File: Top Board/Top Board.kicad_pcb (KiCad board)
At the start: 2 copper layers, 88.9 x 27.9 mm, 5 parts

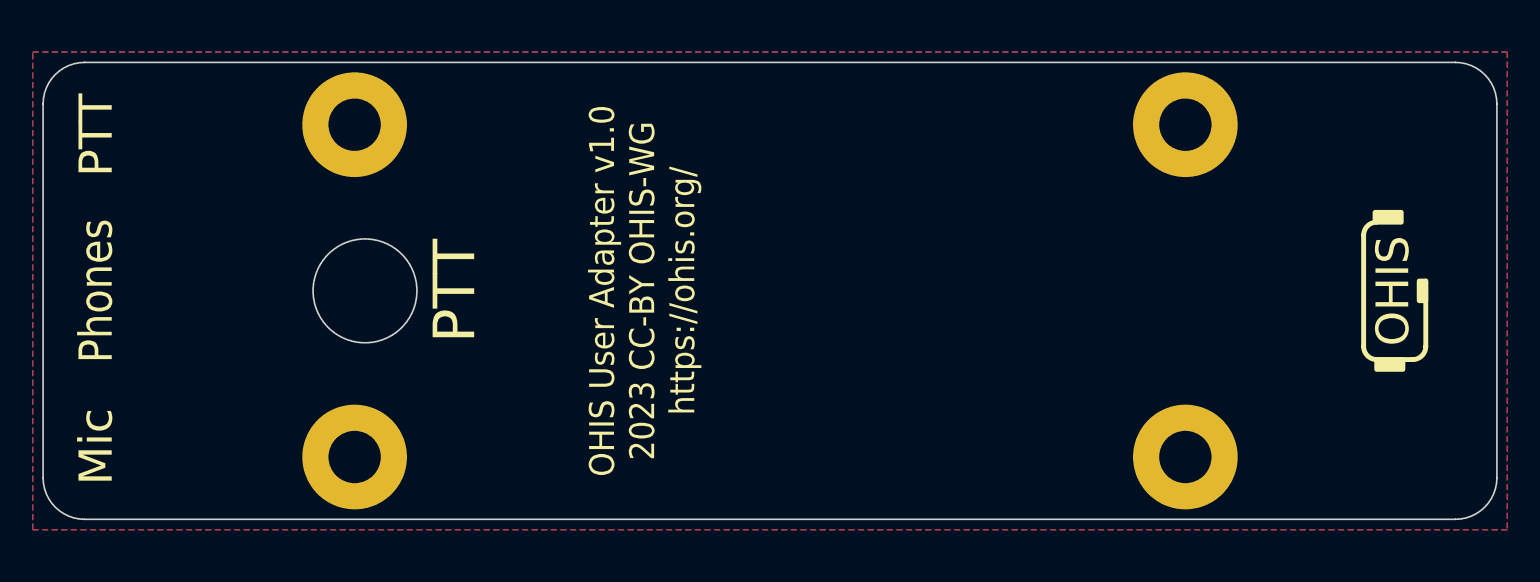
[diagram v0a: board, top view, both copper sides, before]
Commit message: Fixed silkscreen art, added trimpot. #1
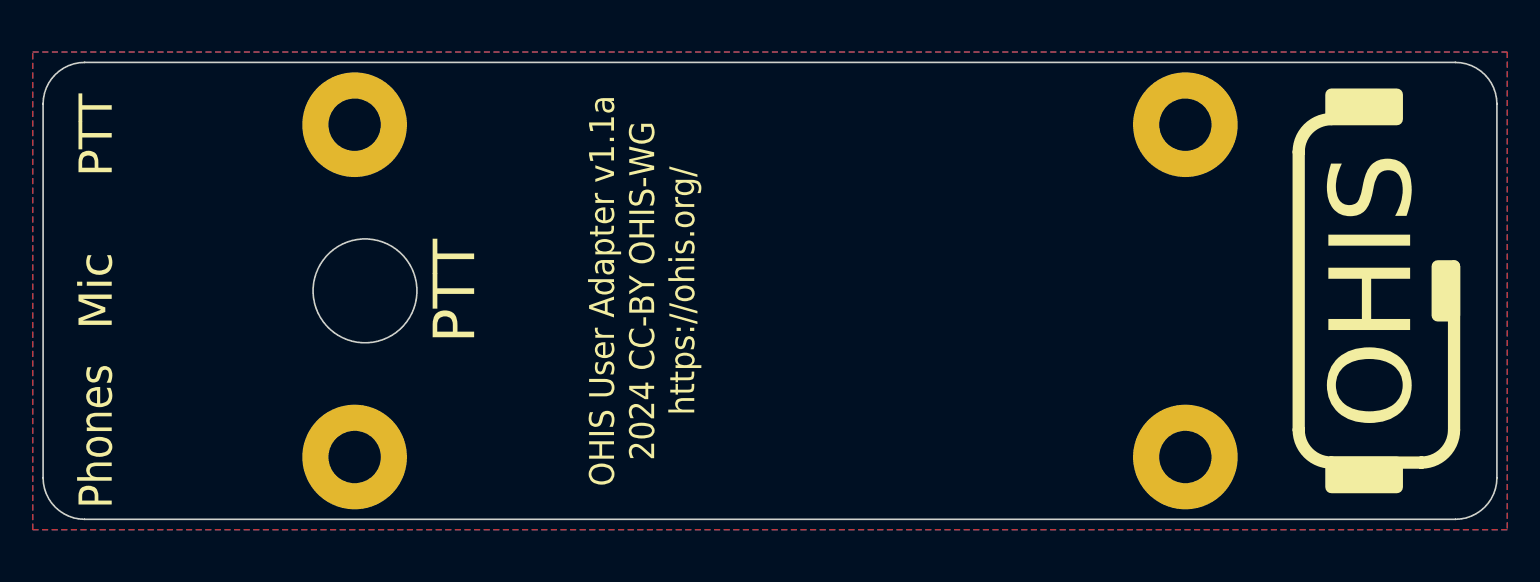
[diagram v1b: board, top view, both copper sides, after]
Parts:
- G1: footprint Libraries:Logo_OHIS_Medium -> Libraries:Logo_OHIS_Large
- moved G1 1.27 mm to (144.8, 76.2)
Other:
- board text added: "JLCJLCJLCJLC"
- board text added: "OHIS User Adapter v1.1a 2024 CC-BY OHIS-WG https://ohis.org/"
- board text removed: "OHIS User Adapter v1.0 2023 CC-BY OHIS-WG https://ohis.org/"
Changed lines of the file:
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@@
       (net 1 "GND") (pinfunction "1") (pintype "input"))
   )
-  (footprint "Libraries:Logo_OHIS_Medium" (layer "F.Cu")
-    (at 146.05 76.2 90)
+  (footprint "Libraries:Logo_OHIS_Large" (layer "F.Cu")
+    (at 144.78 76.2 90)
     (property "Sheetfile" "Top Board.kicad_sch")
     (property "Sheetname" "")
@@
     )
     (fp_text user "OHIS" (at 0 0 90 unlocked) (layer "F.SilkS")
-        (effects (font (size 2 2) (thickness 0.3)))
+        (effects (font (size 5 5) (thickness 0.75)))
     )
     (fp_text user "${REFERENCE}" (at 0 2.5 90 unlocked) (layer "F.Fab") hide
         (effects (font (size 1 1) (thickness 0.15)))
     )
-    (fp_line (start -4.200001 1.2) (end -4.2 -1)
-      (stroke (width 0.3) (type solid)) (layer "F.SilkS"))
-    (fp_line (start 0.6 2) (end -3.400001 2)
-      (stroke (width 0.3) (type solid)) (layer "F.SilkS"))
-    (fp_line (start 3.4 -1.8) (end -3.4 -1.8)
-      (stroke (width 0.3) (type solid)) (layer "F.SilkS"))
-    (fp_rect (start -4.2 0.6) (end -4.8 -1)
-      (stroke (width 0.3) (type solid)) (fill solid) (layer "F.SilkS"))
-    (fp_rect (start 0.6 2) (end -0.6 1.6)
-      (stroke (width 0.3) (type solid)) (fill solid) (layer "F.SilkS"))
-    (fp_rect (start 4.8 0.5) (end 4.2 -1.1)
-      (stroke (width 0.3) (type solid)) (fill solid) (layer "F.SilkS"))
-    (fp_arc (start -4.2 -1) (mid -3.965685 -1.565685) (end -3.4 -1.8)
-      (stroke (width 0.3) (type solid)) (layer "F.SilkS"))
-    (fp_arc (start -3.400001 2) (mid -3.965686 1.765685) (end -4.200001 1.2)
-      (stroke (width 0.3) (type solid)) (layer "F.SilkS"))
-    (fp_arc (start 3.4 -1.8) (mid 3.965685 -1.565685) (end 4.2 -1)
-      (stroke (width 0.3) (type solid)) (layer "F.SilkS"))
+    (fp_line (start -10.5 -2.5) (end -10.5 2.999999)
+      (stroke (width 0.75) (type solid)) (layer "F.SilkS"))
+    (fp_line (start 1.5 5) (end -8.499999 4.999999)
+      (stroke (width 0.75) (type solid)) (layer "F.SilkS"))
+    (fp_line (start 8.499999 -4.499999) (end -8.5 -4.5)
+      (stroke (width 0.75) (type solid)) (layer "F.SilkS"))
+    (fp_rect (start -10.5 -2.5) (end -12 1.5)
+      (stroke (width 0.75) (type solid)) (fill solid) (layer "F.SilkS"))
+    (fp_rect (start 1.5 4) (end -1.5 5)
+      (stroke (width 0.75) (type solid)) (fill solid) (layer "F.SilkS"))
+    (fp_rect (start 11.999999 -2.499999) (end 10.499999 1.500001)
+      (stroke (width 0.75) (type solid)) (fill solid) (layer "F.SilkS"))
+    (fp_arc (start -10.5 -2.5) (mid -9.914214 -3.914214) (end -8.5 -4.5)
+      (stroke (width 0.75) (type solid)) (layer "F.SilkS"))
+    (fp_arc (start -8.499999 4.999999) (mid -9.914213 4.414213) (end -10.499999 2.999999)
+      (stroke (width 0.75) (type solid)) (layer "F.SilkS"))
+    (fp_arc (start 8.499999 -4.499999) (mid 9.914213 -3.914213) (end 10.499999 -2.499999)
+      (stroke (width 0.75) (type solid)) (layer "F.SilkS"))
   )
   (footprint "MountingHole:MountingHole_3.2mm_M3_Pad" locked (layer "F.Cu")
@@
   (gr_arc locked (start 149.86 62.23) (mid 151.656051 62.973949) (end 152.4 64.77)
     (stroke (width 0.1) (type default)) (layer "Edge.Cuts"))
-  (gr_text "Mic" (at 67.945 85.725 90) (layer "F.SilkS")
+  (gr_text "JLCJLCJLCJLC" (at 107.95 76.2) (layer "B.SilkS")
+    (effects (font (size 1.524 1.397) (thickness 0.2032)) (justify mirror))
+  )
+  (gr_text "Mic" (at 67.945 76.2 90) (layer "F.SilkS")
     (effects (font (size 2.032 2.032) (thickness 0.254)) (justify bottom))
   )
-  (gr_text "OHIS User Adapter v1.0\n2023 CC-BY OHIS-WG\nhttps://ohis.org/" (at 103.505 76.2 90) (layer "F.SilkS")
+  (gr_text "OHIS User Adapter v1.1a\n2024 CC-BY OHIS-WG\nhttps://ohis.org/" (at 103.505 76.2 90) (layer "F.SilkS")
     (effects (font (size 1.524 1.397) (thickness 0.2032)) (justify bottom))
   )
-  (gr_text "Phones" (at 67.945 76.2 90) (layer "F.SilkS")
+  (gr_text "Phones" (at 67.945 85.09 90) (layer "F.SilkS")
     (effects (font (size 2.032 1.778) (thickness 0.254)) (justify bottom))
   )

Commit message: Cleaned up board, moved jumpers to right-angle at board edge.
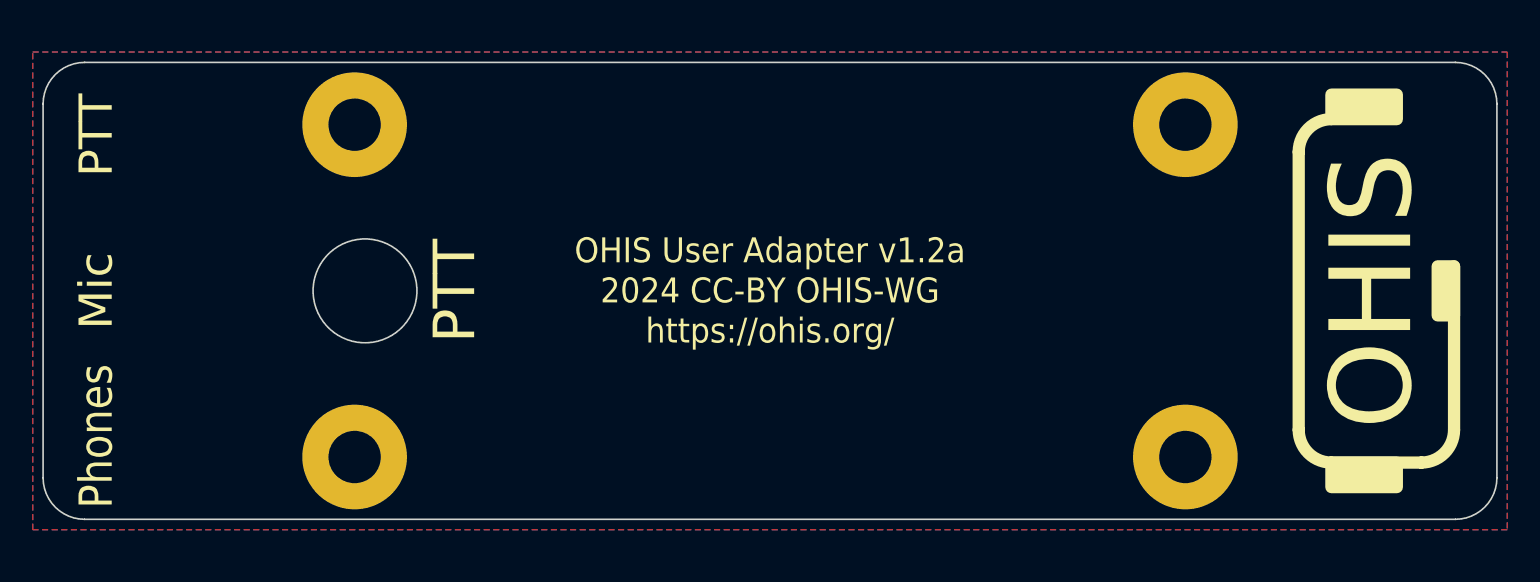
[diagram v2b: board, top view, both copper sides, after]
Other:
- board text added: "OHIS User Adapter v1.2a 2024 CC-BY OHIS-WG https://ohis.org/"
- board text removed: "OHIS User Adapter v1.1a 2024 CC-BY OHIS-WG https://ohis.org/"
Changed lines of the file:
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@@
       (net 1 "GND") (pinfunction "1") (pintype "input"))
   )
-  (gr_rect (start 140.335 67.945) (end 151.13 84.455)
+  (gr_rect (start 140.335 67.945) (end 152.4 84.455)
     (stroke (width 0.15) (type solid)) (fill solid) (layer "B.Mask"))
   (gr_line (start 158.115 76.2) (end 57.15 76.2)
@@
     (effects (font (size 2.032 2.032) (thickness 0.254)) (justify bottom))
   )
-  (gr_text "OHIS User Adapter v1.1a\n2024 CC-BY OHIS-WG\nhttps://ohis.org/" (at 103.505 76.2 90) (layer "F.SilkS")
-    (effects (font (size 1.524 1.397) (thickness 0.2032)) (justify bottom))
+  (gr_text "OHIS User Adapter v1.2a\n2024 CC-BY OHIS-WG\nhttps://ohis.org/" (at 107.95 76.2) (layer "F.SilkS")
+    (effects (font (size 1.524 1.397) (thickness 0.2032)))
   )
   (gr_text "Phones" (at 67.945 85.09 90) (layer "F.SilkS")
@@
     (pts (xy 83.185 76.2) (xy 63.5 76.2))
     (height 17.78)
-    (gr_text "0.7750 in" (at 73.3425 57.27) (layer "Dwgs.User")
+    (gr_text "19.6850 mm" (at 73.3425 57.27) (layer "Dwgs.User")
       (effects (font (size 1 1) (thickness 0.15)))
     )
@@
     (pts (xy 63.5 76.2) (xy 63.5 85.725))
     (height 2.54)
-    (gr_text "0.3750 in" (at 59.81 80.9625 90) (layer "Dwgs.User")
+    (gr_text "9.5250 mm" (at 59.81 80.9625 90) (layer "Dwgs.User")
       (effects (font (size 1 1) (thickness 0.15)))
     )
@@
     (pts (xy 63.5 76.2) (xy 63.5 66.675))
     (height -2.54)
-    (gr_text "0.3750 in" (at 59.81 71.4375 90) (layer "Dwgs.User")
+    (gr_text "9.5250 mm" (at 59.81 71.4375 90) (layer "Dwgs.User")
       (effects (font (size 1 1) (thickness 0.15)))
     )

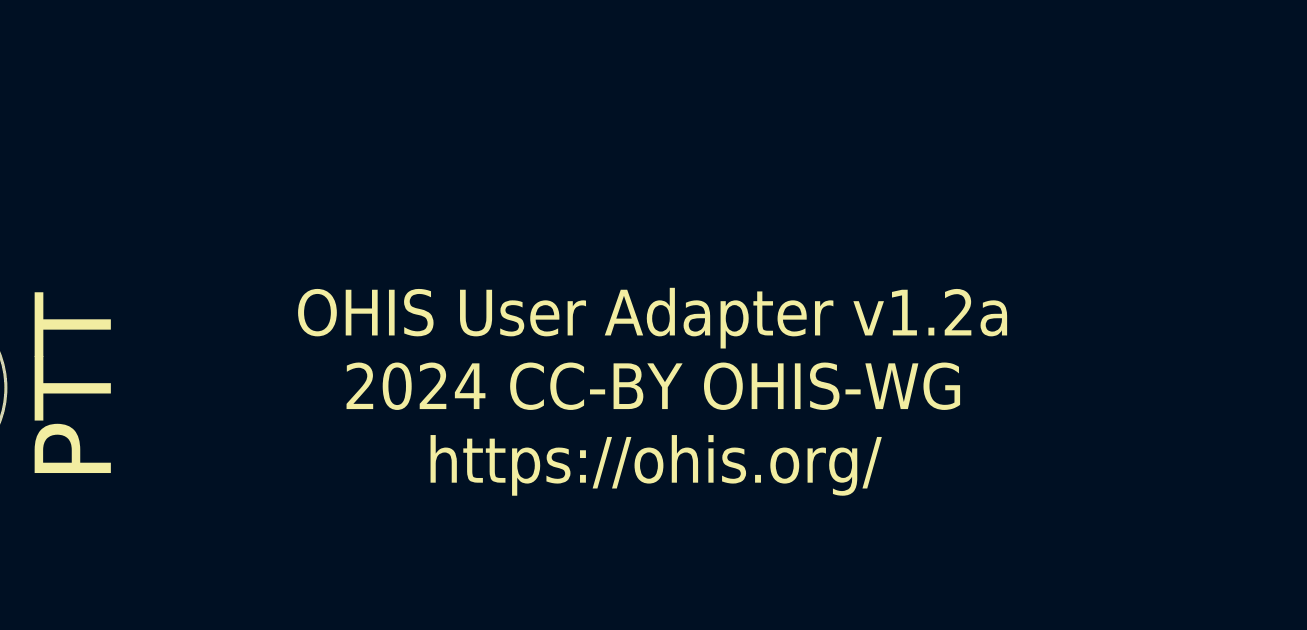
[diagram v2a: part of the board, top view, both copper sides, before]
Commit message: Halibut ordering next batch. Upping version on top/bottom to v1.3a. KiCAD 8.0
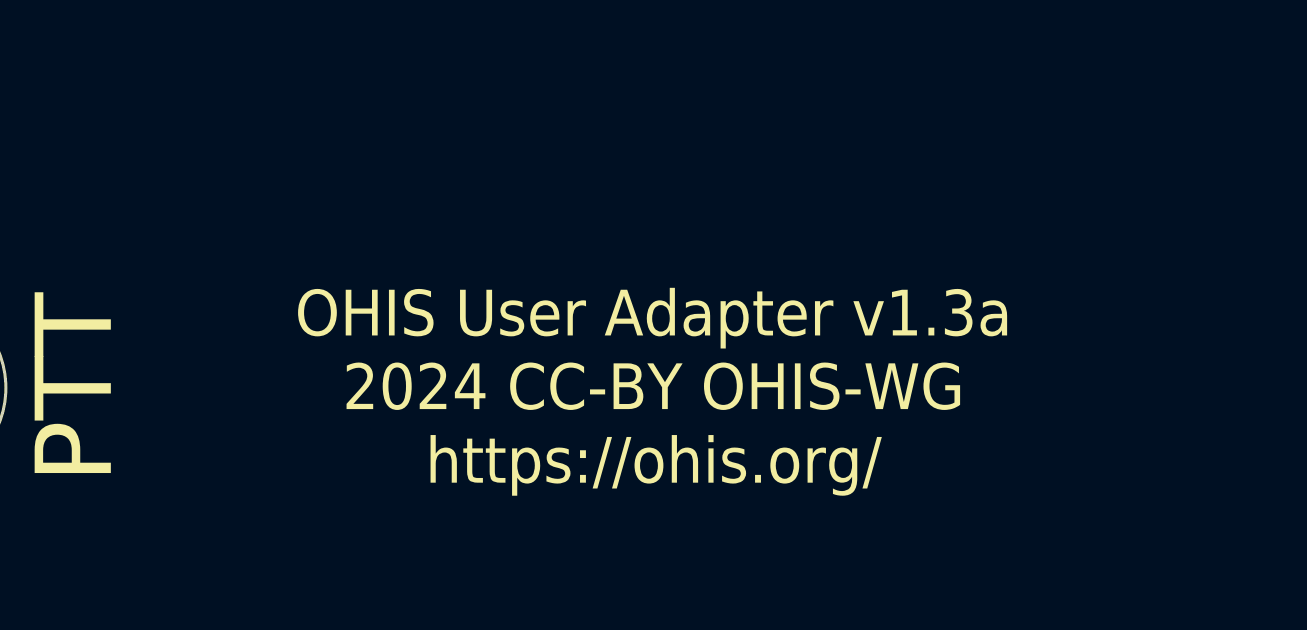
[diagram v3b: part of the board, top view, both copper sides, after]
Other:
- board text added: "OHIS User Adapter v1.3a 2024 CC-BY OHIS-WG https://ohis.org/"
- board text removed: "OHIS User Adapter v1.2a 2024 CC-BY OHIS-WG https://ohis.org/"
